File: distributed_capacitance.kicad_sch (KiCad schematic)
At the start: 21 parts

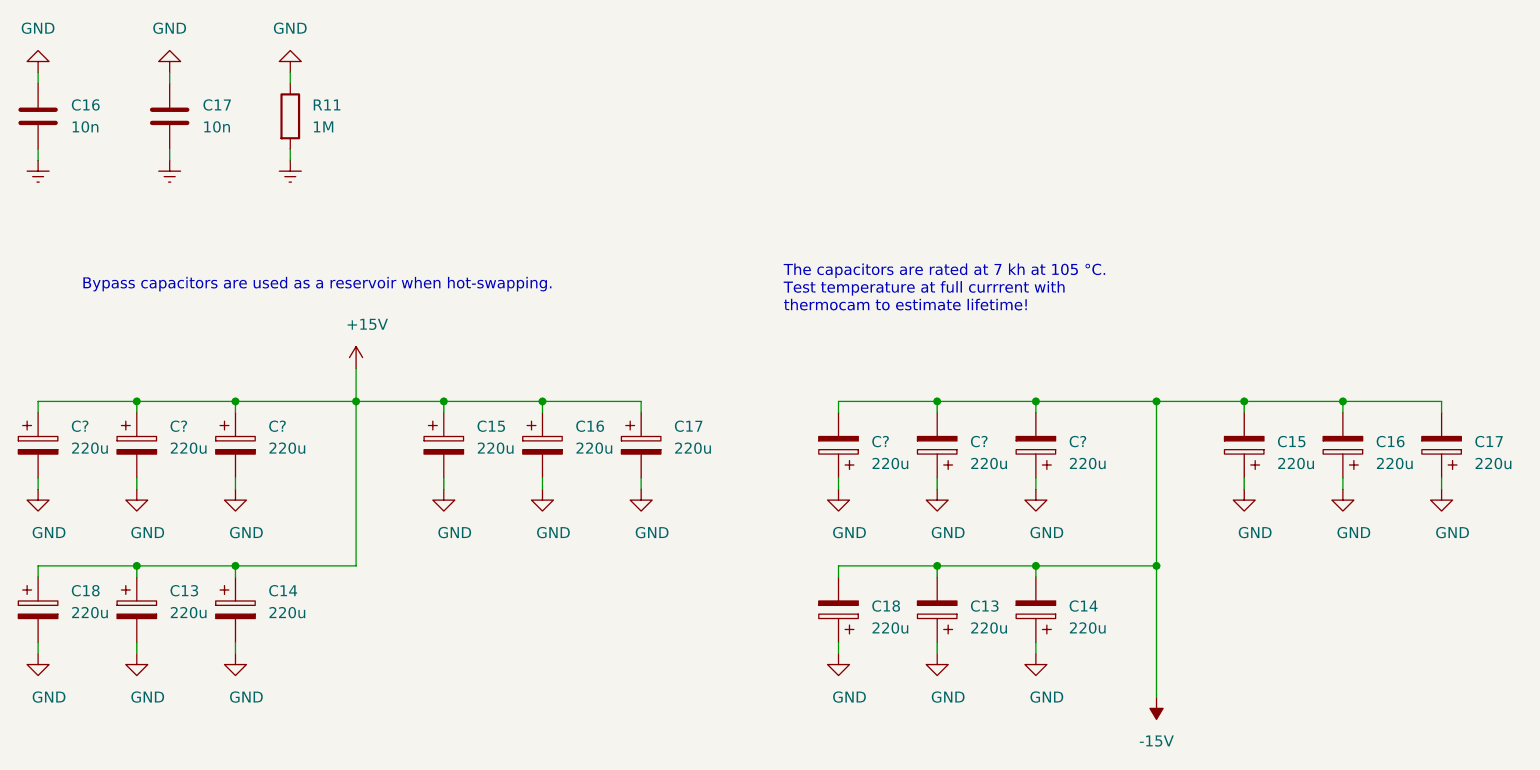
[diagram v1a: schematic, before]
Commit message: Replaced constant current diode with KiCad device available as of v7.0.10 Updated LM5067 3D model
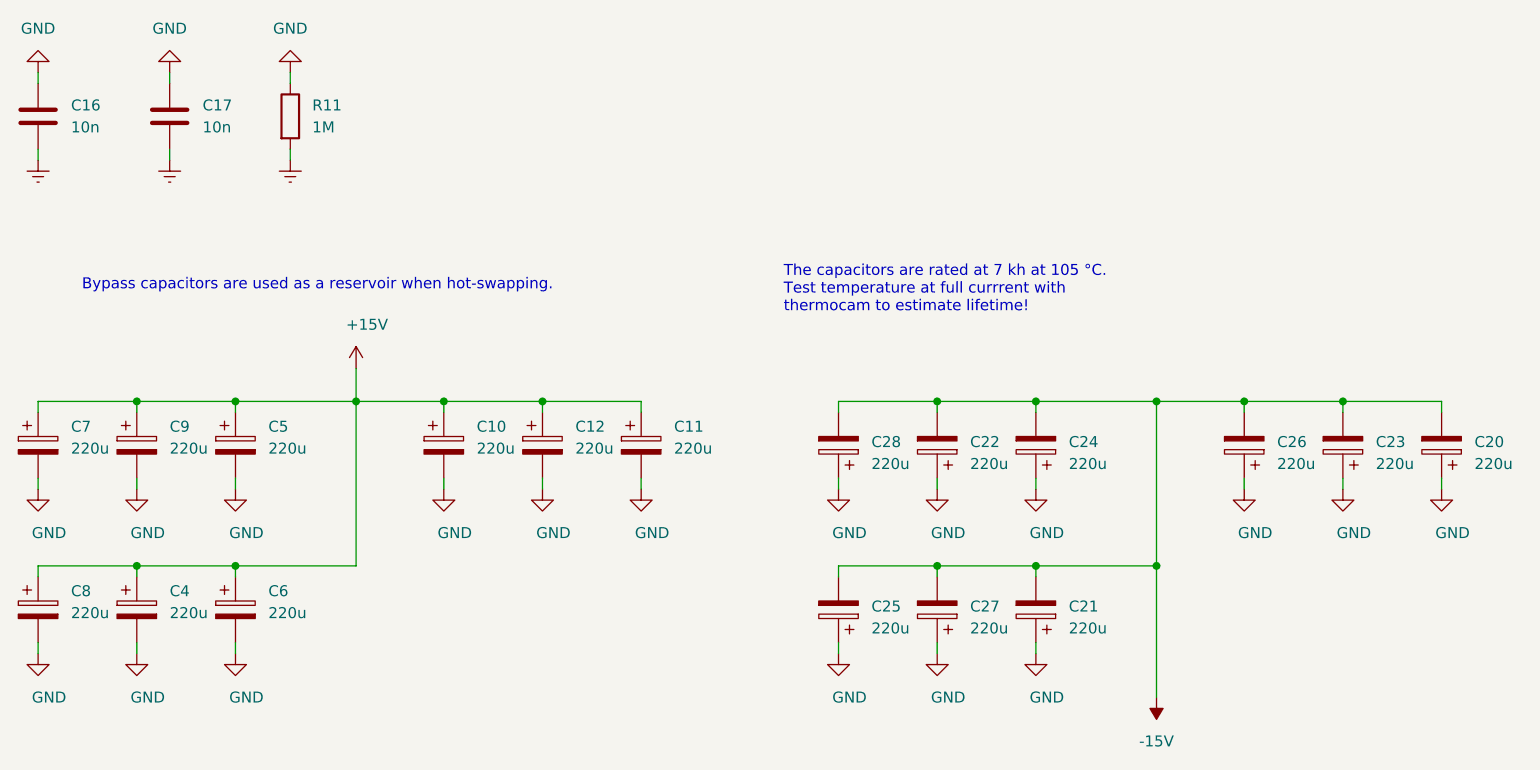
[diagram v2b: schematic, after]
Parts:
- gave numbers to parts that had none: 6
- renumbered C15 to C10, C17 to C11, C16 to C12, C17 to C20, C14 to C21, C16 to C23, C18 to C25, C15 to C26, C13 to C27, C13 to C4, C14 to C6, C18 to C8

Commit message: Updated layout to improve handling flexing of the PCB Changed MLCCs to flexible termination Removed thermal jumper
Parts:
- C16, C17: PN C0603C103K2RECAUTO -> C0603X103K2RECAUTO; digikey# 399-14191-1-ND -> 399-14200-1-ND
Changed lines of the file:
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@@
       (effects (font (size 1.27 1.27)) hide)
     )
-    (property "PN" "C0603C103K2RECAUTO" (at 43.18 63.5 0)
+    (property "PN" "C0603X103K2RECAUTO" (at 43.18 63.5 0)
       (effects (font (size 1.27 1.27)) hide)
     )
@@
       (effects (font (size 1.27 1.27)) hide)
     )
-    (property "digikey#" "399-14191-1-ND" (at 43.18 63.5 0)
+    (property "digikey#" "399-14200-1-ND" (at 43.18 63.5 0)
       (effects (font (size 1.27 1.27)) hide)
     )
@@
       (effects (font (size 1.27 1.27)) hide)
     )
-    (property "PN" "C0603C103K2RECAUTO" (at 58.42 63.5 0)
+    (property "PN" "C0603X103K2RECAUTO" (at 58.42 63.5 0)
       (effects (font (size 1.27 1.27)) hide)
     )
@@
       (effects (font (size 1.27 1.27)) hide)
     )
-    (property "digikey#" "399-14191-1-ND" (at 58.42 63.5 0)
+    (property "digikey#" "399-14200-1-ND" (at 58.42 63.5 0)
       (effects (font (size 1.27 1.27)) hide)
     )
